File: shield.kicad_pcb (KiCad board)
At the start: 2 copper layers, 100 x 80 mm, 0 parts

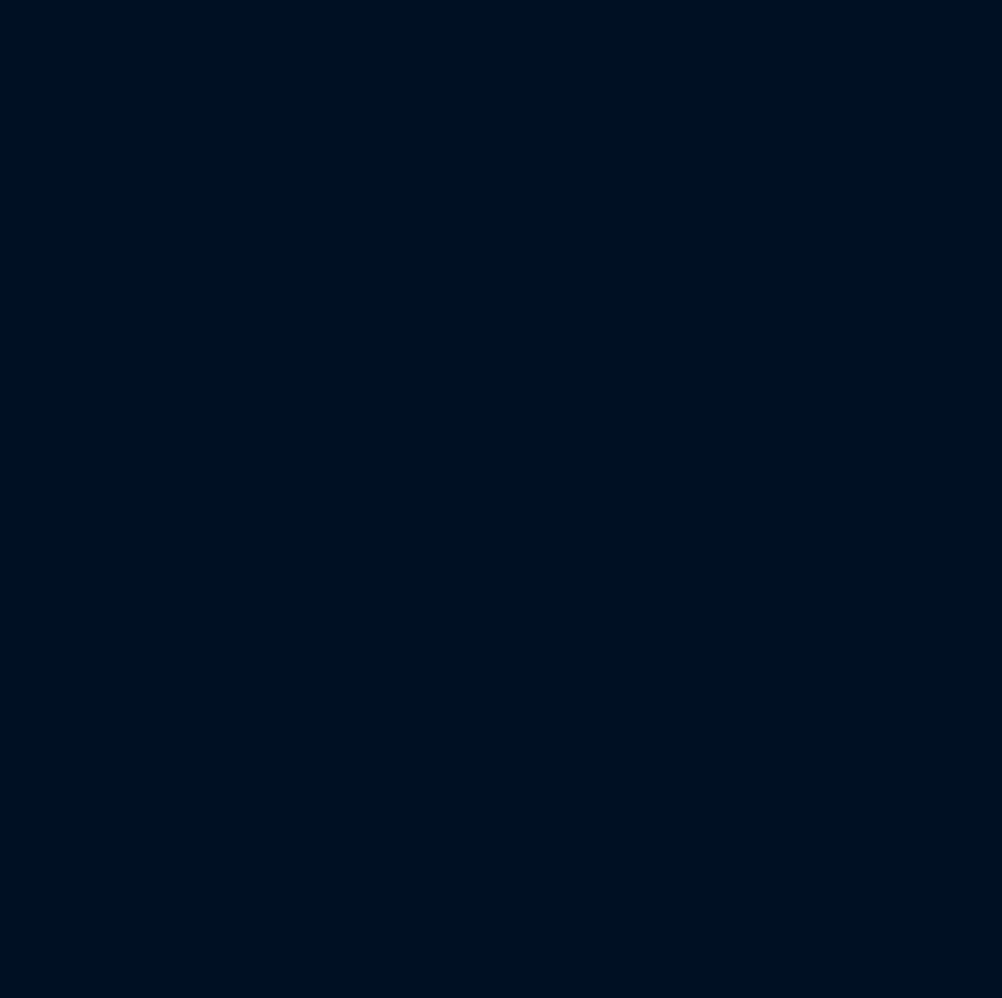
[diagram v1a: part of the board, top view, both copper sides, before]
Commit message: Ajoute l'embase OLED (J10, IDC 2x8 detrompee) et le README du depot
Cree le symbole OLED_SPI_2x8 d'apres le plan constructeur de l'ecran
ER-OLEDM032-1B et le raccorde aux labels SPI deja presents sur les broches
natives de l'ESP32. Documente le choix dans decisions.md (#15) et
nappes-shield.md, et ajoute le README.md qui manquait a ce depot.

Co-Authored-By: Claude Sonnet 5 <noreply@anthropic.com>
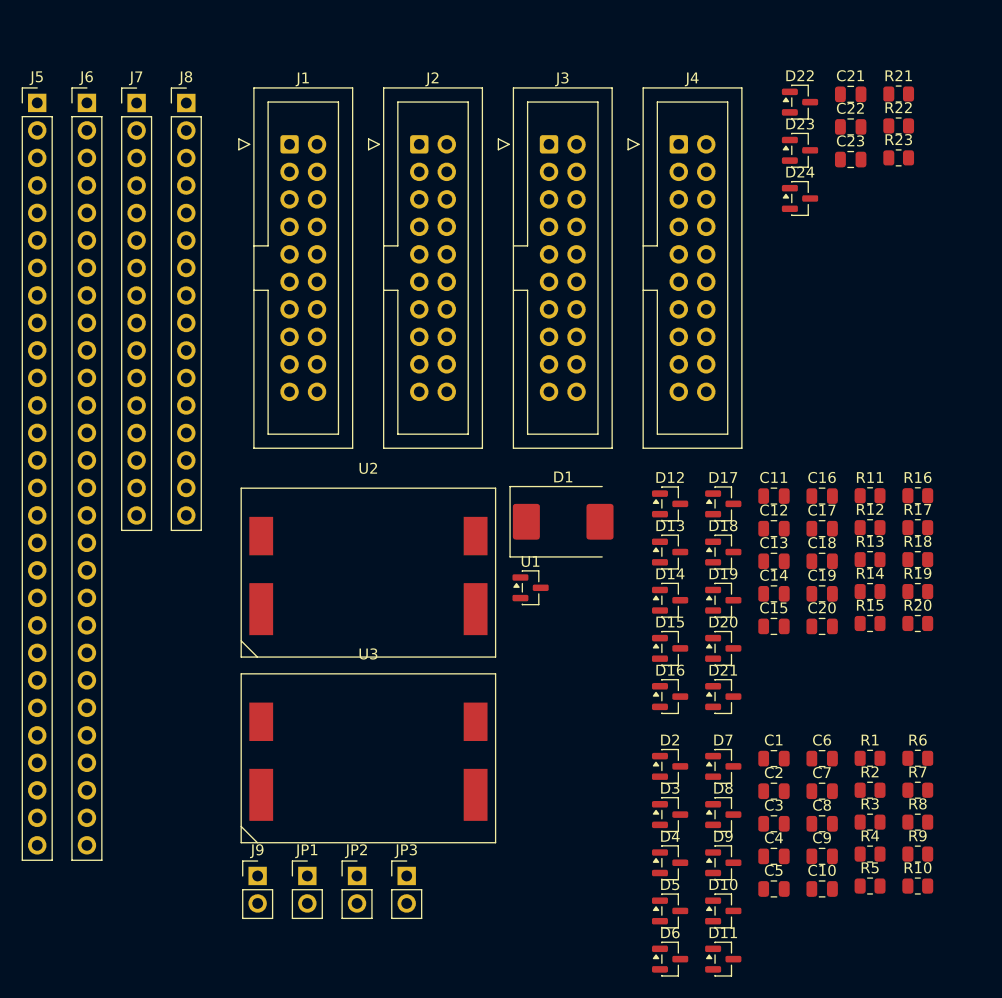
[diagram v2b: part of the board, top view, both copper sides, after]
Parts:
- added C1: 100pF, Capacitor_SMD:C_0805_2012Metric, F.Cu at (88.8, 279.0)
- added C10: 100pF, Capacitor_SMD:C_0805_2012Metric, F.Cu at (93.3, 291.0)
- added C11: 100pF, Capacitor_SMD:C_0805_2012Metric, F.Cu at (88.8, 254.7)
- added C12: 100pF, Capacitor_SMD:C_0805_2012Metric, F.Cu at (88.8, 257.7)
- added C13: 100pF, Capacitor_SMD:C_0805_2012Metric, F.Cu at (88.8, 260.7)
- added C14: 100pF, Capacitor_SMD:C_0805_2012Metric, F.Cu at (88.8, 263.7)
- added C15: 100pF, Capacitor_SMD:C_0805_2012Metric, F.Cu at (88.8, 266.8)
- added C16: 100pF, Capacitor_SMD:C_0805_2012Metric, F.Cu at (93.3, 254.7)
- added C17: 100pF, Capacitor_SMD:C_0805_2012Metric, F.Cu at (93.3, 257.7)
- added C18: 100pF, Capacitor_SMD:C_0805_2012Metric, F.Cu at (93.3, 260.7)
- added C19: 100pF, Capacitor_SMD:C_0805_2012Metric, F.Cu at (93.3, 263.7)
- added C2: 100pF, Capacitor_SMD:C_0805_2012Metric, F.Cu at (88.8, 282.0)
- added C20: 100pF, Capacitor_SMD:C_0805_2012Metric, F.Cu at (93.3, 266.8)
- added C21: 100pF, Capacitor_SMD:C_0805_2012Metric, F.Cu at (95.9, 217.6)
- added C22: 100pF, Capacitor_SMD:C_0805_2012Metric, F.Cu at (95.9, 220.6)
- added C23: 100pF, Capacitor_SMD:C_0805_2012Metric, F.Cu at (95.9, 223.6)
- added C3: 100pF, Capacitor_SMD:C_0805_2012Metric, F.Cu at (88.8, 285.0)
- added C4: 100pF, Capacitor_SMD:C_0805_2012Metric, F.Cu at (88.8, 288.0)
- added C5: 100pF, Capacitor_SMD:C_0805_2012Metric, F.Cu at (88.8, 291.0)
- added C6: 100pF, Capacitor_SMD:C_0805_2012Metric, F.Cu at (93.3, 279.0)
- added C7: 100pF, Capacitor_SMD:C_0805_2012Metric, F.Cu at (93.3, 282.0)
- added C8: 100pF, Capacitor_SMD:C_0805_2012Metric, F.Cu at (93.3, 285.0)
- added C9: 100pF, Capacitor_SMD:C_0805_2012Metric, F.Cu at (93.3, 288.0)
- added D1: D_Zener_3V3_ISO_protect, Diode_SMD:D_SMC, F.Cu at (69.4, 257.1)
- added D10: BAT54S, Package_TO_SOT_SMD:SOT-23, F.Cu at (84.2, 293.0)
- added D11: BAT54S, Package_TO_SOT_SMD:SOT-23, F.Cu at (84.2, 297.5)
- added D12: BAT54S, Package_TO_SOT_SMD:SOT-23, F.Cu at (79.3, 255.4)
- added D13: BAT54S, Package_TO_SOT_SMD:SOT-23, F.Cu at (79.3, 259.9)
- added D14: BAT54S, Package_TO_SOT_SMD:SOT-23, F.Cu at (79.3, 264.3)
- added D15: BAT54S, Package_TO_SOT_SMD:SOT-23, F.Cu at (79.3, 268.8)
- added D16: BAT54S, Package_TO_SOT_SMD:SOT-23, F.Cu at (79.3, 273.2)
- added D17: BAT54S, Package_TO_SOT_SMD:SOT-23, F.Cu at (84.2, 255.4)
- added D18: BAT54S, Package_TO_SOT_SMD:SOT-23, F.Cu at (84.2, 259.9)
- added D19: BAT54S, Package_TO_SOT_SMD:SOT-23, F.Cu at (84.2, 264.3)
- added D2: BAT54S, Package_TO_SOT_SMD:SOT-23, F.Cu at (79.3, 279.7)
- added D20: BAT54S, Package_TO_SOT_SMD:SOT-23, F.Cu at (84.2, 268.8)
- added D21: BAT54S, Package_TO_SOT_SMD:SOT-23, F.Cu at (84.2, 273.2)
- added D22: BAT54S, Package_TO_SOT_SMD:SOT-23, F.Cu at (91.3, 218.3)
- added D23: BAT54S, Package_TO_SOT_SMD:SOT-23, F.Cu at (91.3, 222.8)
- added D24: BAT54S, Package_TO_SOT_SMD:SOT-23, F.Cu at (91.3, 227.2)
- added D3: BAT54S, Package_TO_SOT_SMD:SOT-23, F.Cu at (79.3, 284.1)
- added D4: BAT54S, Package_TO_SOT_SMD:SOT-23, F.Cu at (79.3, 288.6)
- added D5: BAT54S, Package_TO_SOT_SMD:SOT-23, F.Cu at (79.3, 293.0)
- added D6: BAT54S, Package_TO_SOT_SMD:SOT-23, F.Cu at (79.3, 297.5)
- added D7: BAT54S, Package_TO_SOT_SMD:SOT-23, F.Cu at (84.2, 279.7)
- added D8: BAT54S, Package_TO_SOT_SMD:SOT-23, F.Cu at (84.2, 284.1)
- added D9: BAT54S, Package_TO_SOT_SMD:SOT-23, F.Cu at (84.2, 288.6)
- added J1: NAPPE_ADC1, Connector_IDC:IDC-Header_2x10_P2.54mm_Vertical, F.Cu at (44.1, 222.2)
- added J2: NAPPE_ADC2, Connector_IDC:IDC-Header_2x10_P2.54mm_Vertical, F.Cu at (56.1, 222.2)
- added J3: NAPPE_PWM, Connector_IDC:IDC-Header_2x10_P2.54mm_Vertical, F.Cu at (68.1, 222.2)
- added J4: NAPPE_GPIO, Connector_IDC:IDC-Header_2x10_P2.54mm_Vertical, F.Cu at (80.1, 222.2)
- added J5: DEVKIT_C2000_ROW_A, Connector_PinHeader_2.54mm:PinHeader_1x28_P2.54mm_Vertical, F.Cu at (20.8, 218.4)
- added J6: DEVKIT_C2000_ROW_B, Connector_PinHeader_2.54mm:PinHeader_1x28_P2.54mm_Vertical, F.Cu at (25.4, 218.4)
- added J7: ESP32_C6_DEVKITC_1_J1, Connector_PinHeader_2.54mm:PinHeader_1x16_P2.54mm_Vertical, F.Cu at (30.0, 218.4)
- added J8: ESP32_C6_DEVKITC_1_J3, Connector_PinHeader_2.54mm:PinHeader_1x16_P2.54mm_Vertical, F.Cu at (34.6, 218.4)
- added J9: J_PWR_11-25V, Connector_PinHeader_2.54mm:PinHeader_1x02_P2.54mm_Vertical, F.Cu at (41.2, 289.8)
- added JP1: Cavalier_E-S, Connector_PinHeader_2.54mm:PinHeader_1x02_P2.54mm_Vertical, F.Cu at (45.7, 289.8)
- added JP2: Cavalier_C2000, Connector_PinHeader_2.54mm:PinHeader_1x02_P2.54mm_Vertical, F.Cu at (50.3, 289.8)
- added JP3: Cavalier_ESP32, Connector_PinHeader_2.54mm:PinHeader_1x02_P2.54mm_Vertical, F.Cu at (54.9, 289.8)
- added R1: 100R, Resistor_SMD:R_0805_2012Metric, F.Cu at (97.7, 278.9)
- added R10: 100R, Resistor_SMD:R_0805_2012Metric, F.Cu at (102.1, 290.7)
- added R11: 100R, Resistor_SMD:R_0805_2012Metric, F.Cu at (97.7, 254.7)
- added R12: 100R, Resistor_SMD:R_0805_2012Metric, F.Cu at (97.7, 257.6)
- added R13: 100R, Resistor_SMD:R_0805_2012Metric, F.Cu at (97.7, 260.6)
- added R14: 100R, Resistor_SMD:R_0805_2012Metric, F.Cu at (97.7, 263.5)
- added R15: 100R, Resistor_SMD:R_0805_2012Metric, F.Cu at (97.7, 266.5)
- added R16: 100R, Resistor_SMD:R_0805_2012Metric, F.Cu at (102.1, 254.7)
- added R17: 100R, Resistor_SMD:R_0805_2012Metric, F.Cu at (102.1, 257.6)
- added R18: 100R, Resistor_SMD:R_0805_2012Metric, F.Cu at (102.1, 260.6)
- added R19: 100R, Resistor_SMD:R_0805_2012Metric, F.Cu at (102.1, 263.5)
- added R2: 100R, Resistor_SMD:R_0805_2012Metric, F.Cu at (97.7, 281.9)
- added R20: 100R, Resistor_SMD:R_0805_2012Metric, F.Cu at (102.1, 266.5)
- added R21: 100R, Resistor_SMD:R_0805_2012Metric, F.Cu at (100.4, 217.6)
- added R22: 100R, Resistor_SMD:R_0805_2012Metric, F.Cu at (100.4, 220.5)
- added R23: 100R, Resistor_SMD:R_0805_2012Metric, F.Cu at (100.4, 223.5)
- added R3: 100R, Resistor_SMD:R_0805_2012Metric, F.Cu at (97.7, 284.8)
- added R4: 100R, Resistor_SMD:R_0805_2012Metric, F.Cu at (97.7, 287.8)
- added R5: 100R, Resistor_SMD:R_0805_2012Metric, F.Cu at (97.7, 290.7)
- added R6: 100R, Resistor_SMD:R_0805_2012Metric, F.Cu at (102.1, 278.9)
- added R7: 100R, Resistor_SMD:R_0805_2012Metric, F.Cu at (102.1, 281.9)
- added R8: 100R, Resistor_SMD:R_0805_2012Metric, F.Cu at (102.1, 284.8)
- added R9: 100R, Resistor_SMD:R_0805_2012Metric, F.Cu at (102.1, 287.8)
- added U1: LDO_3V3_ISO, Package_TO_SOT_SMD:SOT-23, F.Cu at (66.4, 263.2)
- added U2: NCM3S1205MC, lib:NCM3S1205MC, F.Cu at (51.4, 261.8)
- added U3: NCM3S1205MC, lib:NCM3S1205MC, F.Cu at (51.4, 278.9)

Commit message: Regles de clearance par domaine d'isolement et filtre EMC recommande sur les NCM3S1205MC
Ajoute deux netclasses (Isole_Primaire/Isole_Secondaire, assignees par nom
de net) et une regle shield.kicad_dru qui impose 8mm de clearance des
qu'une paire traverse les deux domaines - valeur issue du datasheet
Murata (UL62368-1, 2 MOPP, 250Vrms), pas estimee. Rien n'existait avant
pour differencier electriquement primaire et secondaire au DRC.

Ajoute le filtre EMC recommande par le datasheet (p.8) sur l'entree des
deux NCM3S1205MC (L1-L4, C26-C35), ce qui a necessite de renommer les
labels VIN_PWR/GND_PRI au niveau des pins VIN de U2/U3 vers des noeuds
intermediaires dedies (U2_VINF/U2_GNDF, U3_VINF/U3_GNDF).

Co-Authored-By: Claude Sonnet 5 <noreply@anthropic.com>
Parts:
- added J10: OLED_SPI_2x8, Connector_IDC:IDC-Header_2x08_P2.54mm_Vertical, F.Cu at (127.0, 41.6)
- moved JP1 239.0 mm to (171.6, 86.7)
- moved J2 233.3 mm to (226.6, 63.1)
- moved J1 232.8 mm to (210.9, 59.8)
- moved J9 222.6 mm to (129.8, 85.7)
- moved JP3 222.4 mm to (185.6, 109.8)
- moved JP2 217.2 mm to (172.0, 109.9)
- moved J8 209.9 mm to (99.8, 19.0)
- moved J7 204.9 mm to (77.0, 19.0)
- moved J6 201.6 mm to (45.7, 17.8)
- moved J3 201.1 mm to (227.4, 99.6)
- moved J5 200.6 mm to (22.9, 17.8)
- moved U2 199.6 mm to (151.9, 89.4)
- moved U3 193.8 mm to (151.5, 113.0)
- moved J4 178.7 mm to (212.1, 101.8)
- moved D1 36.2 mm to (53.1, 224.7), turned to 180 degrees
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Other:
- board outline removed

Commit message: Gabarit de netclasses, filtre EMC NCM3S1205MC, embase OLED, et groupement/routage des 23 trios de protection
- shield.kicad_pro : 8 netclasses (Default/Rapide/Analogique/Alim/Isole_Primaire/
  Isole_Secondaire/Puissance/HT), 83 motifs de net classes
- dc.kicad_sch : filtre EMC d'entree (L1-L4, C26-C28, C31-C33) pour les deux
  NCM3S1205MC ; etage de sortie (C4/C5 du datasheet) volontairement omis
  (decision #16, doc/decisions.md)
- connecteur_devkit.kicad_sch : embase OLED J10 (IDC 2x8 detrompee),
  symbole mecanique U4 (ER-OLEDM032-1), correction label 3V3_ESP32
- shield.kicad_pcb : les 23 trios de protection (BAT54S+R+C) groupes,
  routes (GND + signal interne), retournes en B.Cu pour matcher le
  gabarit, places en couronne hors carte pour placement/routage manuel
- doc/nappes-shield.md, doc/decisions.md : mis a jour en consequence

Co-Authored-By: Claude Sonnet 5 <noreply@anthropic.com>
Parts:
- added C24: 100nF, Capacitor_SMD:C_0805_2012Metric, F.Cu at (253.8, 248.7)
- added C25: 100nF, Capacitor_SMD:C_0805_2012Metric, F.Cu at (253.8, 251.7)
- added C26: 22uF, Capacitor_SMD:C_0805_2012Metric, F.Cu at (253.8, 254.7)
- added C27: 22uF, Capacitor_SMD:C_0805_2012Metric, F.Cu at (253.8, 257.7)
- added C28: 220pF, Capacitor_SMD:C_0805_2012Metric, F.Cu at (253.8, 260.7)
- added C29: 470pF, Capacitor_SMD:C_0805_2012Metric, F.Cu at (258.3, 248.7)
- added C30: 470pF, Capacitor_SMD:C_0805_2012Metric, F.Cu at (258.3, 251.7)
- added C31: 22uF, Capacitor_SMD:C_0805_2012Metric, F.Cu at (258.3, 254.7)
- added C32: 22uF, Capacitor_SMD:C_0805_2012Metric, F.Cu at (258.3, 257.7)
- added C33: 220pF, Capacitor_SMD:C_0805_2012Metric, F.Cu at (258.3, 260.7)
- added C34: 470pF, Capacitor_SMD:C_0805_2012Metric, F.Cu at (262.7, 248.7)
- added C35: 470pF, Capacitor_SMD:C_0805_2012Metric, F.Cu at (262.7, 251.7)
- added C36: 100uF, Capacitor_SMD:C_1210_3225Metric, F.Cu at (184.0, 80.0)
- added C37: 100uF, Capacitor_SMD:C_1210_3225Metric, F.Cu at (131.0, 113.0)
- added C38: 10uF, Capacitor_SMD:C_0805_2012Metric, F.Cu at (262.7, 254.7)
- added C39: 10uF, Capacitor_SMD:C_0805_2012Metric, F.Cu at (262.7, 257.7)
- added C40: 100uF 50V, Capacitor_SMD:CP_Elec_8x10.5, F.Cu at (195.5, 46.2)
- added C41: 100uF 50V, Capacitor_SMD:CP_Elec_8x10.5, F.Cu at (195.5, 60.9)
- added L1: 22uH, Inductor_SMD:L_0805_2012Metric, B.Cu at (272.9, 263.6)
- added L2: 22uH, Inductor_SMD:L_0805_2012Metric, F.Cu at (245.4, 248.8)
- added L3: 22uH, Inductor_SMD:L_0805_2012Metric, F.Cu at (245.4, 251.5)
- added L4: 22uH, Inductor_SMD:L_0805_2012Metric, F.Cu at (245.4, 254.2)
- added U4: ER-OLEDM032-1, lib:ER-OLEDM032-1, F.Cu at (181.9, 52.2)
- C1, C10, C11, C12, C13, C14, C15, C16, C17, C18, C19, C2, C20, C21, C22, C23, C3, C4, C5, C6, C7, C8, C9, D10, D11, D12, D13, D14, D15, D16, D17, D18, D19, D2, D20, D21, D22, D23, D24, D3, D4, D5, D6, D7, D8, D9, R1, R10, R11, R12, R13, R14, R15, R16, R17, R18, R19, R2, R20, R21, R22, R23, R3, R4, R5, R6, R7, R8, R9: moved to B.Cu
- moved D10 302.2 mm to (190.0, 10.0)
- moved R5 302.0 mm to (209.1, 10.1), turned to 180 degrees
- moved D7 295.5 mm to (205.0, 10.0)
- moved R9 292.6 mm to (194.1, 10.1), turned to 180 degrees
- moved C9 291.0 mm to (190.0, 13.6)
- moved D8 288.8 mm to (175.0, 10.0)
- moved C6 288.0 mm to (205.0, 13.6)
- moved D11 286.7 mm to (252.0, 65.0)
- moved R8 285.4 mm to (179.1, 10.1), turned to 180 degrees
- moved C8 283.5 mm to (175.0, 13.6)
- moved D14 279.2 mm to (252.0, 45.0)
- moved C10 273.3 mm to (252.0, 68.5)
- moved R10 273.2 mm to (256.1, 65.0), turned to 180 degrees
- moved C13 267.7 mm to (252.0, 48.5)
- moved R13 267.4 mm to (256.1, 45.0), turned to 180 degrees
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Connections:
- J10 pad 2: 5V_ESP32 -> 3V3_ESP32
- J7 pad 1: unconnected-(J7-3V3-Pad1) -> 3V3_ESP32
- U2 pad 1: VIN_PWR -> U2_VINF
- U2 pad 2: GND_PRI -> U2_GNDF
- U3 pad 1: VIN_PWR -> U3_VINF
- U3 pad 2: GND_PRI -> U3_GNDF
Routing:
- net GND: track 0.00 -> 59.7 mm
- net nFAULT_MCU: track 0.00 -> 5.76 mm
- net Temp2_MCU: track 0.00 -> 5.76 mm
- net PWM3_A_MCU: track 0.00 -> 5.76 mm
- net PWM2_B_MCU: track 0.00 -> 5.76 mm
- net PWM2_A_MCU: track 0.00 -> 5.76 mm
- net PWM1_B_MCU: track 0.00 -> 5.76 mm
- net PWM1_A_MCU: track 0.00 -> 5.76 mm
- net Iin_MCU: track 0.00 -> 5.76 mm
- net I_shunt2_MCU: track 0.00 -> 5.76 mm
- net I_shunt1_MCU: track 0.00 -> 5.76 mm
- net I2C_SDA_MCU: track 0.00 -> 5.76 mm
- net I2C_SCL_MCU: track 0.00 -> 5.76 mm
- net VREF_ADC_MCU: track 0.00 -> 5.76 mm
- net VREFLO_SENSE_MCU: track 0.00 -> 5.76 mm
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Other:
- board outline added: 120 x 120 mm
- copper layers 2 -> 4
